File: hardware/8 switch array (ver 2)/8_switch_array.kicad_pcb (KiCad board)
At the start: 2 copper layers, 45.5 x 71 mm, 35 parts, among them J1 Conn_01x04, J10 Conn_01x02, J11 Conn_01x02, J2 Conn_01x04, J3 Conn_01x02, J4 Conn_01x02, J5 Conn_01x02, J6 Conn_01x02, J7 Conn_01x02, J8 Conn_01x02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

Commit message: update 8 switch array
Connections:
- J1 pad 1: +5V -> SER_IN
- J1 pad 2: GND -> RCLK
- J1 pad 3: SER_IN -> +5V
- J1 pad 4: RCLK -> GND
- J2 pad 1: Net-(J2-Pad1) -> SRCLK
- J2 pad 2: GND -> SRCLR
- J2 pad 3: SRCLK -> Net-(J2-Pad3)
- J2 pad 4: SRCLR -> GND
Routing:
- net +5V: track 13.2 -> 26.7 mm
- net RCLK: track 10.8 -> 14.2 mm
- net SER_IN: track 9.74 -> 11.8 mm
- net SRCLK: track 10.7 -> 9.17 mm
- net SRCLR: track 10.6 -> 9.19 mm

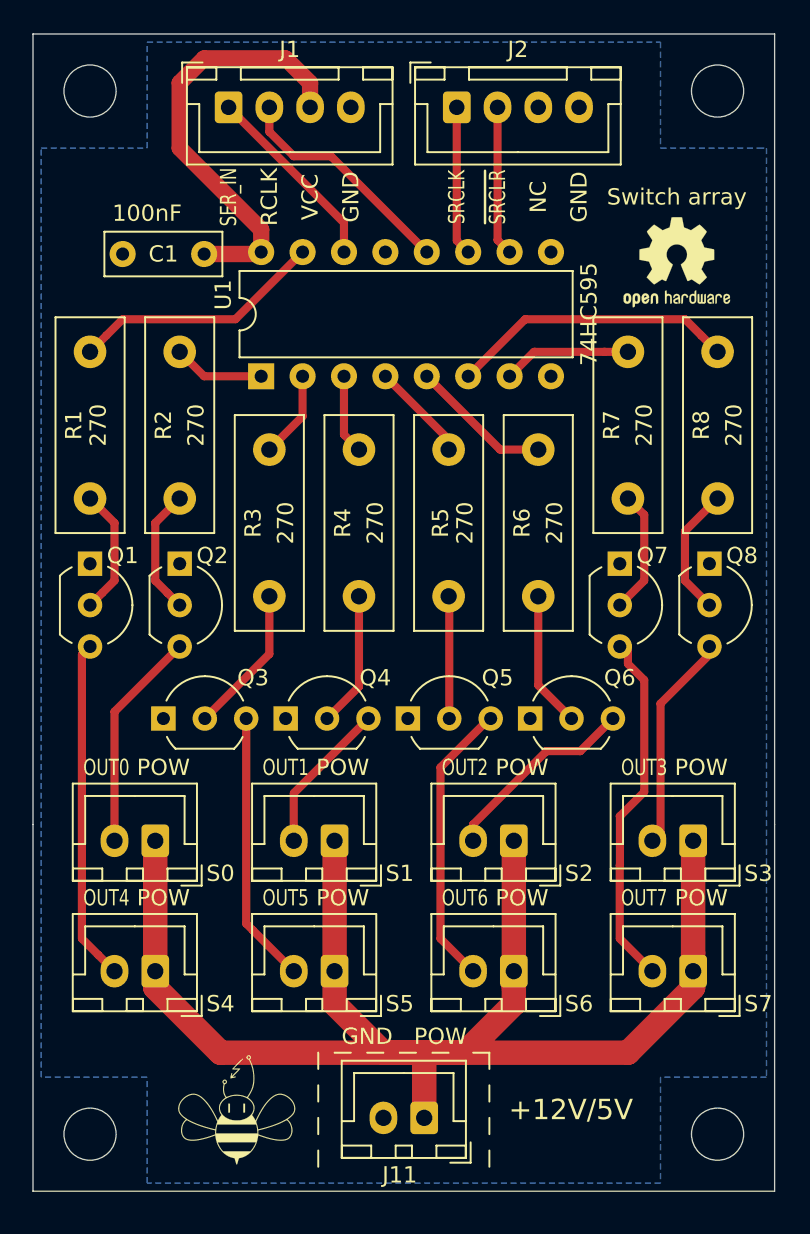
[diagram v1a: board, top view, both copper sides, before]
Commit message: Update on 12V5A system power line
- 12V5A power line is now represented by two connectors with 2 pins across all the modules
- all .png previews are updated. The central hub now has previews for schematics, PCB tracing and 3D model
- peltier module now has two 12V5A connectors with redesigned one side of the bridge. Now all MOSFETs can be equipped with heatsinks
- hum/temp sensor now has its connector position reversed to mimic Grove's one
- hum/temp and gas sensors now have a small BeeHive logo on front layer rather than one big on back layer
- hum/temp sensor now use only one layer for signals and one layer for ground
- switch arrays now have two connectors for 12V5A and 5V3A power lines
- switch arrays had their power lines better traced (no sharp turns)
- power supply (12V5A to 5V3A) now has two connectors for 12V5A power line
- one trace of power supply, which lies in between LM2596's legs, was narrowed to ensure that it will not be accidentally soldered or damaged during placement
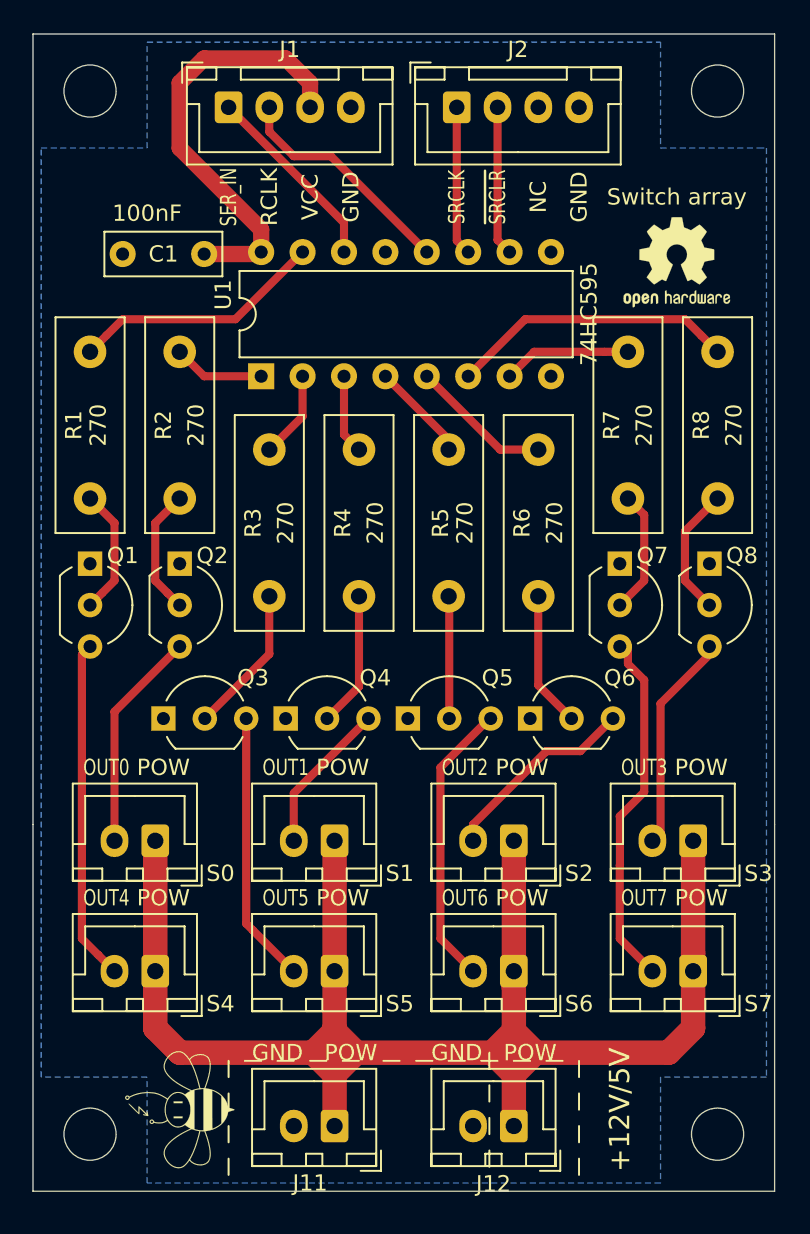
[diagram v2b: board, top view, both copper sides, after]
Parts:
- added J12: Conn_01x02, Connector_JST:JST_XH_B2B-XH-A_1x02_P2.50mm_Vertical, F.Cu at (153.5, 100.5)
- moved J11 5.52 mm to (142.5, 100.5)
- moved G*** 3.50 mm to (133.0, 99.5), turned to 90 degrees
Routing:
- net +12V: track 92.8 -> 110.2 mm
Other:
- rule pad_to_mask_clearance: 0.051 -> 0

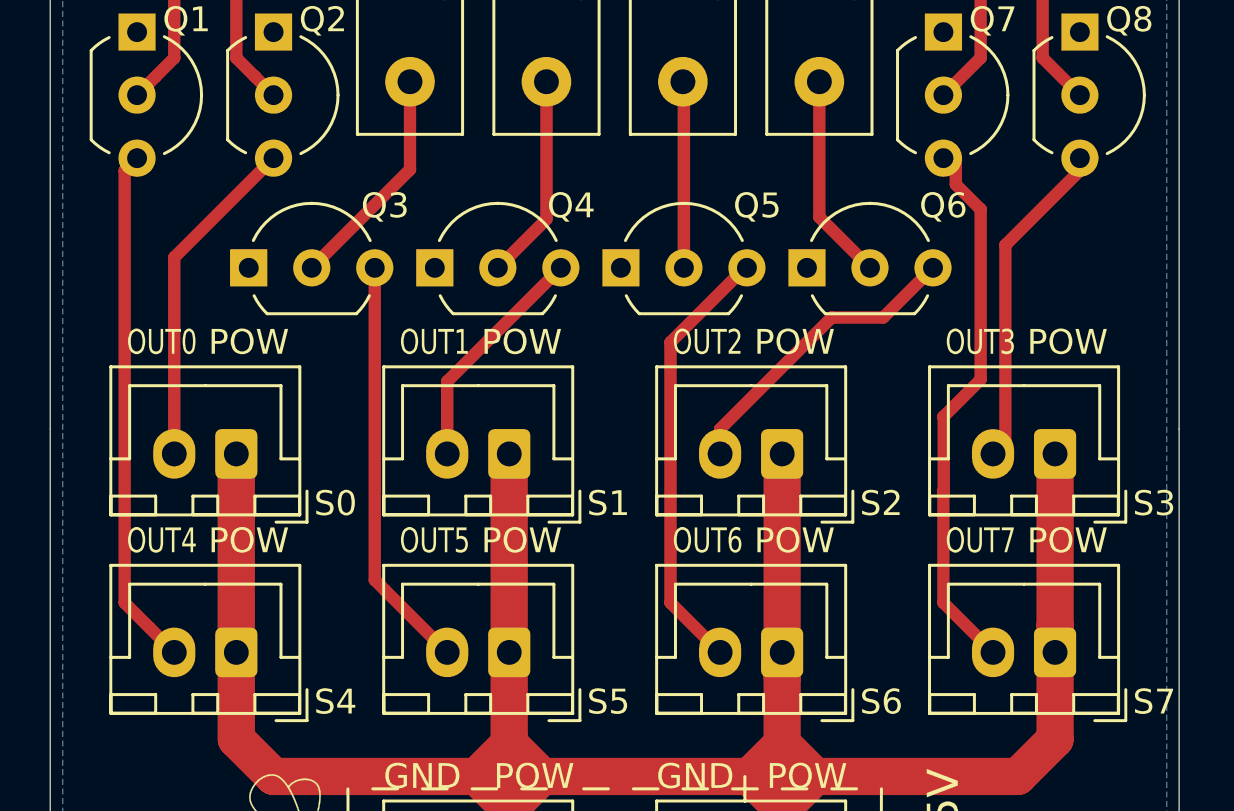
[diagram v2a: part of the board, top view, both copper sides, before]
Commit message: Add high power switch and change 4 switch array
- added high power switch
- removed shift register from 4 switch array
- changed some references on silk layer
- small changes in switch arrays' tracing (width and paths)
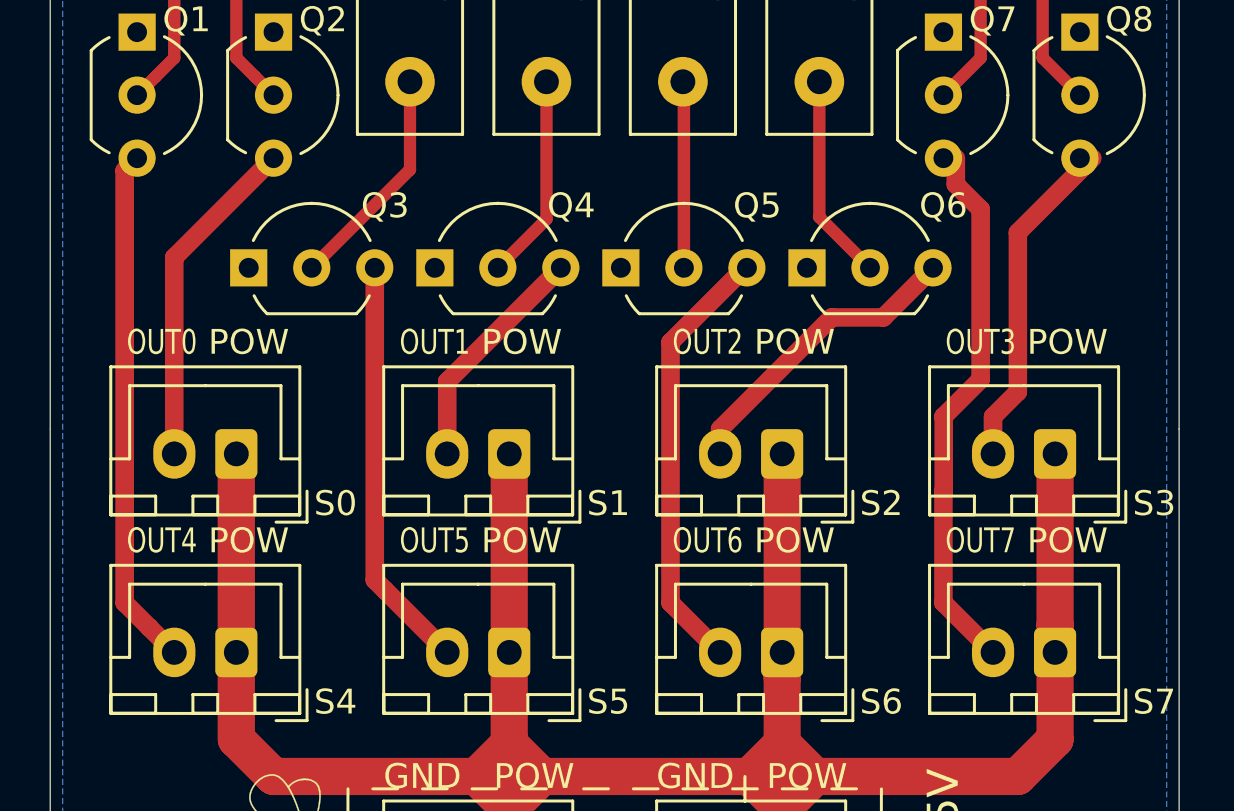
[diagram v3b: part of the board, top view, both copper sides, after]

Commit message: Add version number to boards
Add version number to boards and update screenshots, zip gerber archives
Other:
- board text added: "v0.2"
